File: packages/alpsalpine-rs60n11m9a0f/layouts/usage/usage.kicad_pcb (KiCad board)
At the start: 2 copper layers, 73 x 20 mm, 27 parts

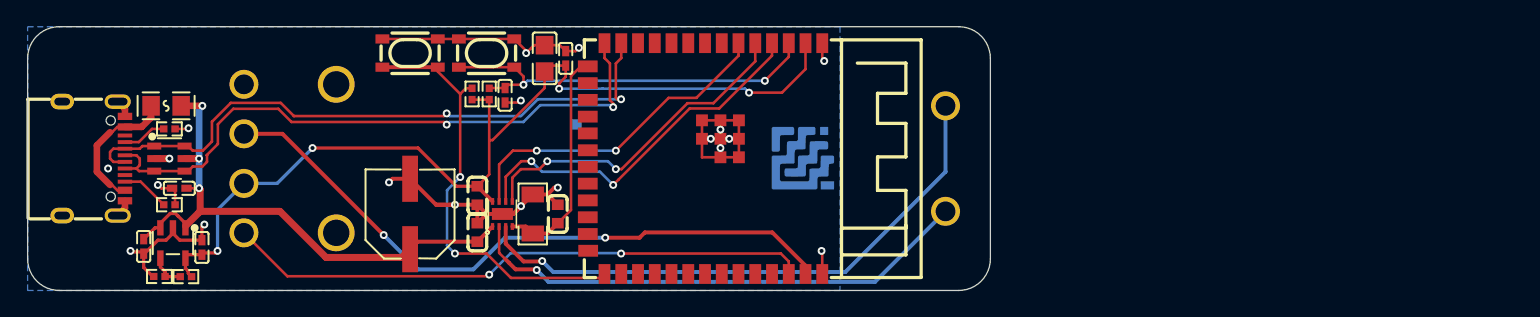
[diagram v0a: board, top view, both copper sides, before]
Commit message: simplify usage and default
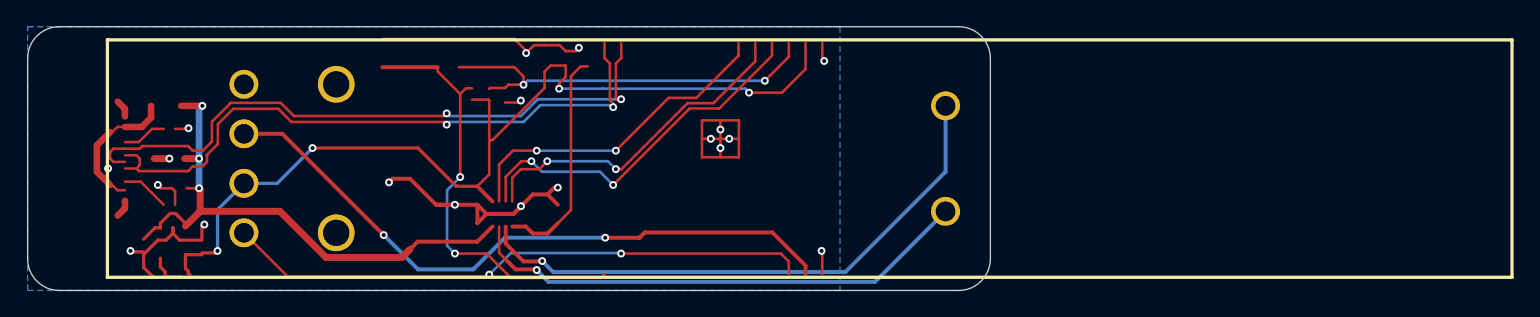
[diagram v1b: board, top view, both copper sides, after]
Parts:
- removed C1: 10µF ±10% 25V X5R, Samsung_Electro_Mechanics_CL21A106KAYNNNE:C0805
- removed C10, C2: 100nF ±10% 16V X7R, Samsung_Electro_Mechanics_CL05B104KO5NNNC:C0402
- removed C3: , Nichicon_UWT1C101MCL1GB:CAP-SMD_BD6.3-L6.6-W6.6-LS7.6-FD
- removed C4, C5, C6: 1µF ±10% 25V X5R, Samsung_Electro_Mechanics_CL05A105KA5NQNC:C0402
- removed C7, C8, C9: 100nF ±10% 50V X7R, YAGEO_CC0603KRX7R9BB104:C0603
- removed D1: , STMicroelectronics_USBLC6_2SC6:SOT-23-6_L2.9-W1.6-P0.95-LS2.8-BL
- removed F1: , BHFUSE_BSMD0805_050_15V:F0805
- removed LOGO1: , atopile_Logo_25x6mm:atopile_Logo_25x6mm
- removed R1, R3, R4: 10kΩ ±1% 62.5mW, UNI_ROYAL_0402WGF1002TCE:R0402
- removed R5: 18kΩ ±1% 62.5mW, UNI_ROYAL_0402WGF1802TCE:R0402
- removed R6: 1Ω ±1% 250mW, UNI_ROYAL_1206W4F100KT5E:R1206
- removed R7, R8: 5.1kΩ ±1% 62.5mW, UNI_ROYAL_0402WGF5101TCE:R0402
- removed SW1, SW2: , ALPSALPINE_SKRPACE010:KEY-SMD_4P-L4.2-W3.2-P2.20-LS4.6
- removed U1: , Texas_Instruments_DRV8210PDSGR:WSON-8_L2.0-W2.0-P0.50-TL-EP
- removed U2: , STMicroelectronics_LDK220M_R:SOT-23-5_L3.0-W1.7-P0.95-LS2.8-BL
- removed U3: , Espressif_Systems_ESP32_S3_WROOM_1_N16R8:WIRELM-SMD_ESP32-S3-WROOM-1
- removed USB1: , SHOU_HAN_TYPE_C_16PIN_2MD_073:USB-C-SMD_TYPE-C-6PIN-2MD-073
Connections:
- R2 pad 1: GND -> lv
- R2 pad 2: POT_SENSE -> line
- R2 pad 3: VCC_LOGIC -> hv
- R2 pad A: A -> motor_out[0]
- R2 pad B: B -> motor_negative
- R2 pad L1: L1 -> L
- R2 pad L2: L2 -> L
- R2 pad T: TOUCH_SENSE -> SIG_T
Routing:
- net lv: track 0.00 -> 75.6 mm, vias 0 -> 19
- net GND: track 75.6 -> 0.00 mm, vias 19 -> 0
- net hv: track 0.00 -> 72.5 mm, vias 0 -> 4
- net VCC_LOGIC: track 72.5 -> 0.00 mm, vias 4 -> 0
- net TOUCH_SENSE: track 49.7 -> 0.00 mm, vias 2 -> 0
- net SIG_T: track 0.00 -> 49.7 mm, vias 0 -> 2
- net USB_D_N: track 49.1 -> 0.00 mm, vias 2 -> 0
- net 3: track 0.00 -> 49.1 mm, vias 0 -> 2
- net USB_D_P: track 48.6 -> 0.00 mm, vias 2 -> 0
- net 41: track 0.00 -> 48.6 mm, vias 0 -> 2
- net line: track 0.00 -> 44.6 mm, vias 0 -> 2
- net POT_SENSE: track 44.6 -> 0.00 mm, vias 2 -> 0
- net motor_out[0]: track 0.00 -> 43.7 mm, vias 0 -> 1
- net A: track 43.7 -> 0.00 mm, vias 1 -> 0
- net VCC_MOTOR: track 42.8 -> 0.00 mm, vias 3 -> 0
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- added copper zone on B.Cu, net lv
- removed copper zone on B.Cu, net GND
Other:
- board text added: "Power Slide GumsticknRay Allen"
- board text removed: "Power Slide Gumstick Ray Allen"

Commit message: building
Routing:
- net lv: track 75.6 -> 31.9 mm, vias 19 -> 14
- net hv: track 72.5 -> 35.3 mm, vias 4 -> 1
- net 8: track 42.8 -> 21.0 mm, vias 3 -> 0
- net 12: track 10.6 -> 0.00 mm
- net 3: track 49.1 -> 41.5 mm
- net 41: track 48.6 -> 42.0 mm
- net 40: track 17.1 -> 13.1 mm
- net 33: track 3.66 -> 0.00 mm
- net 45: track 3.35 -> 0.00 mm
- net 10: track 2.69 -> 0.00 mm

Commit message: fix text
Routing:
- net (no net): track 0.00 -> 260.7 mm, vias 0 -> 14
- net 41: track 42.0 -> 0.00 mm, vias 2 -> 0
- net 3: track 41.5 -> 0.00 mm, vias 2 -> 0
- net 21: track 33.2 -> 0.00 mm, vias 2 -> 0
- net 19: track 30.6 -> 0.00 mm, vias 2 -> 0
- net 4: track 28.3 -> 0.00 mm, vias 2 -> 0
- net 42: track 25.8 -> 0.00 mm, vias 2 -> 0
- net 22: track 25.3 -> 0.00 mm, vias 2 -> 0
- net 8: track 21.0 -> 0.00 mm
- net 40: track 13.1 -> 0.00 mm
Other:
- board text added: "Power Slide Gumstick Ray Allen"
- board text removed: "Power Slide GumsticknRay Allen"
